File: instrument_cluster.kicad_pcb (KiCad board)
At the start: 2 copper layers, 144.8 x 45.7 mm, 76 parts, among them J1 Conn_02x16_Top_Bottom, J2 Conn_02x16_Top_Bottom, J3 USB mini-B SMD, J4 NOT_FITTED_SWD_Conn_01x04_Male, J5 54819-0572, J6 NOT_FITTED_SWD_Conn_01x04_Male, U1 LM2575S-5.0_NOPB, U10 74HC4050D, U11 TJA1040T, U12 TJA1040T, U2 LM2575S-5.0_NOPB, U3 LD1117S33TR_SOT223, U4 LD1117S33TR_SOT223, U5 STM32F105RBTx, U6 TJA1040T, U7 TJA1040T, U8 74HC4050D, U9 STM32F105RBTx, Y1 Crystal KX-13 25MHz, Y2 Crystal KX-13 25MHz

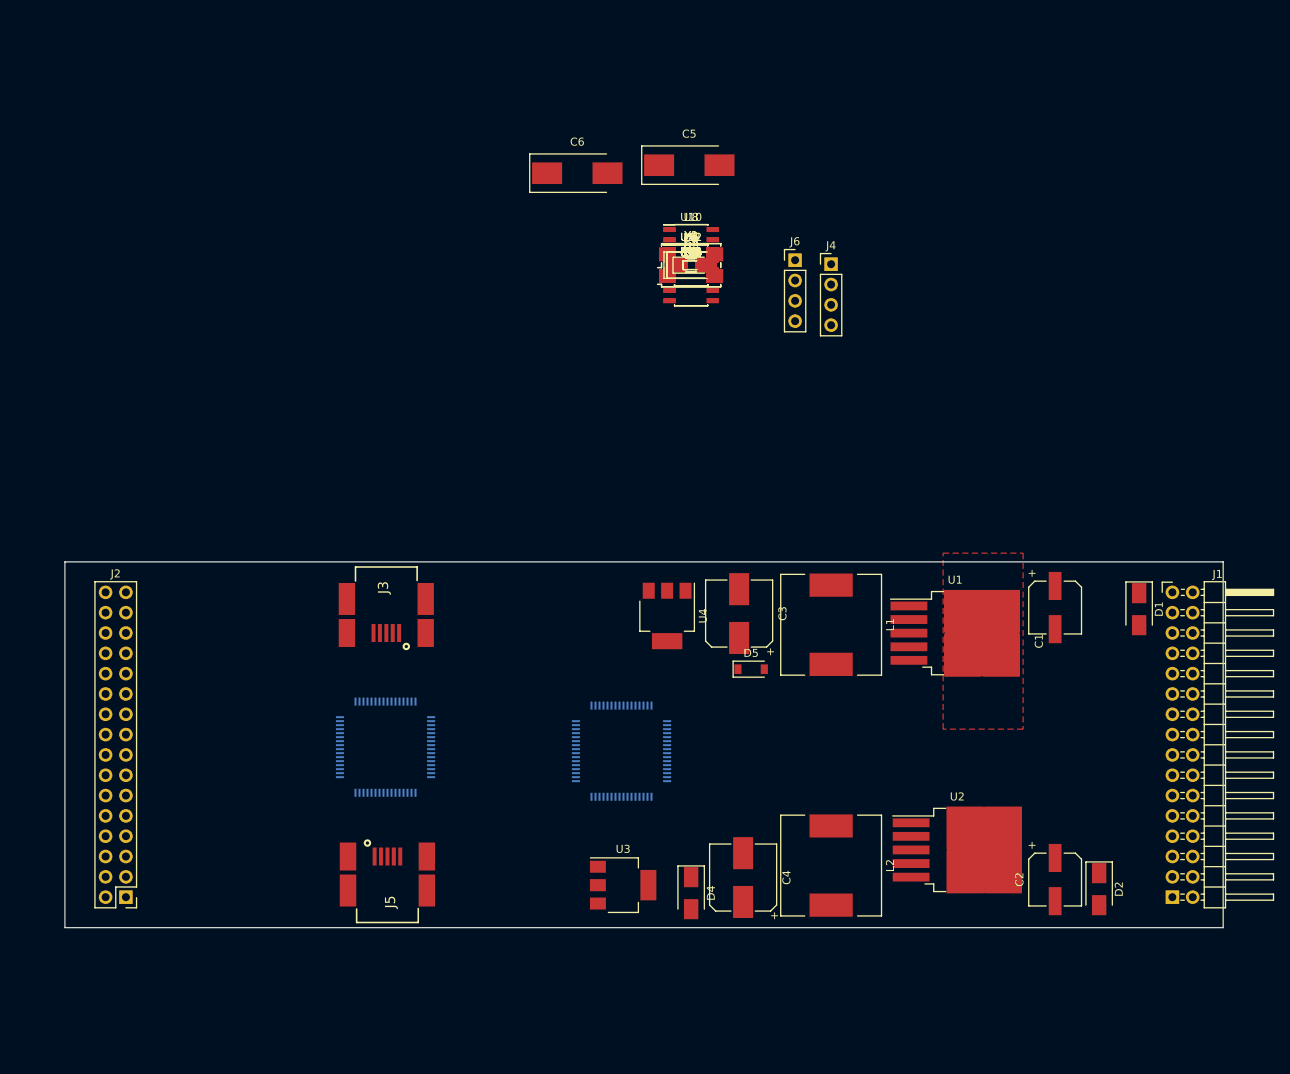
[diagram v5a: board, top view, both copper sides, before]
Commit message: power converters placement complete
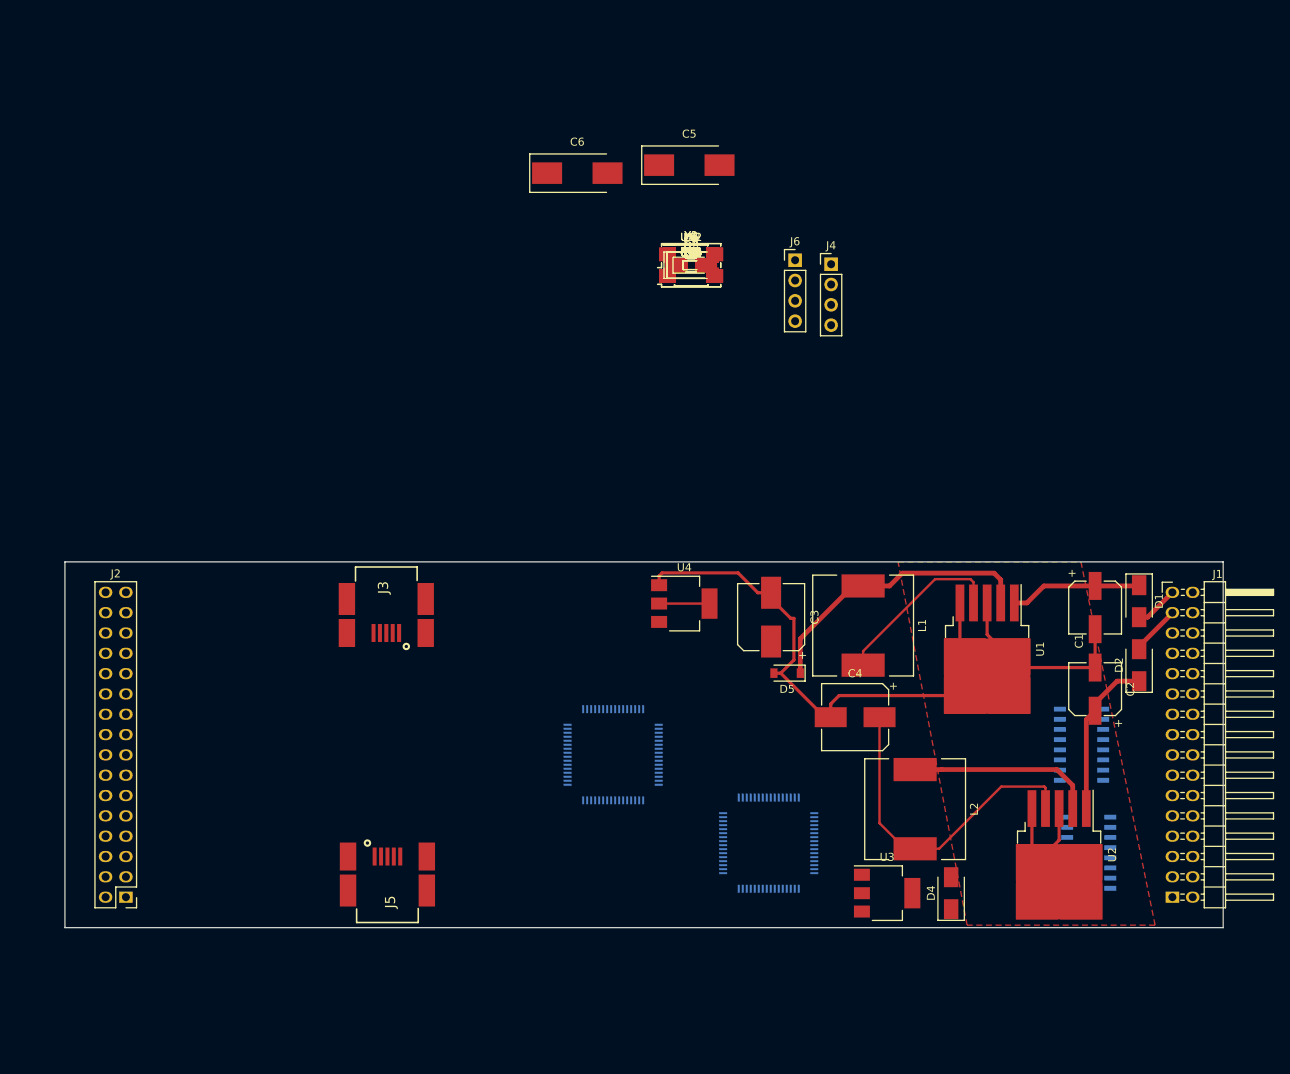
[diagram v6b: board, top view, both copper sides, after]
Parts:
- U10, U8: moved to B.Cu
- moved U8 88.7 mm to (190.2, 121.4), turned to 180 degrees
- moved U10 77.3 mm to (189.3, 107.9), turned to 180 degrees
- moved U9 49.4 mm to (150.2, 120.2)
- moved U3 33.0 mm to (165.0, 126.5)
- moved D4 32.5 mm to (173.0, 126.5), turned to 90 degrees
- moved D2 28.4 mm to (196.5, 98.0), turned to 90 degrees
- moved C4 24.5 mm to (161.0, 104.5), turned to 180 degrees
- moved C2 24.3 mm to (191.0, 101.0), turned to 90 degrees
- moved U2 12.7 mm to (186.5, 121.7), turned to 270 degrees
- moved L2 12.6 mm to (168.5, 116.0)
- moved C1 5.00 mm to (191.0, 90.8)
- moved D5 4.53 mm to (152.5, 99.0), turned to 180 degrees
- moved U1 4.47 mm to (177.5, 96.0), turned to 270 degrees
- moved C3 4.03 mm to (150.5, 92.0)
- moved L1 4.00 mm to (162.0, 93.0)
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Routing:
- net GND: track 0.00 -> 134.7 mm
- net /power_supply/+5V_A_module: track 0.00 -> 41.2 mm
- net Net-(D5-Pad1): track 0.00 -> 36.0 mm
- net Net-(D6-Pad1): track 0.00 -> 23.4 mm
- net /power_supply/+5V_B_module: track 0.00 -> 22.0 mm
- net /power_supply/+12V_A: track 0.00 -> 20.3 mm
- net /FUEL_TANK_in: track 0.00 -> 16.9 mm
- net /+3V3_B: track 0.00 -> 6.30 mm
- net /IGN: track 0.00 -> 6.28 mm
- net /VBATT: track 0.00 -> 5.44 mm

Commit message: change connectivity of level-shifters(on sheme and pcb)
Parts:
- moved U10 6.70 mm to (192.6, 113.8), turned to 270 degrees
- moved U8 2.59 mm to (192.4, 122.8), turned to 270 degrees
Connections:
- J1 pad 10: (no net) -> Net-(J1-Pad10)
- J1 pad 11: (no net) -> Net-(J1-Pad11)
- J1 pad 14: (no net) -> Net-(J1-Pad14)
- J1 pad 20: (no net) -> /RR_FOG
- J1 pad 23: (no net) -> Net-(J1-Pad23)
- J1 pad 24: (no net) -> /FR_FOG
- J1 pad 25: (no net) -> Net-(J1-Pad25)
- J1 pad 26: (no net) -> Net-(J1-Pad26)
- J1 pad 28: (no net) -> Net-(J1-Pad28)
- J1 pad 29: (no net) -> Net-(J1-Pad29)
- J1 pad 30: (no net) -> Net-(J1-Pad30)
- J2 pad 10: (no net) -> Net-(J2-Pad10)
- J2 pad 11: (no net) -> Net-(J2-Pad11)
- J2 pad 13: (no net) -> Net-(J2-Pad13)
- J2 pad 14: (no net) -> Net-(J2-Pad14)
- J2 pad 16: (no net) -> Net-(J2-Pad16)
- J2 pad 17: (no net) -> Net-(J2-Pad17)
- J2 pad 18: (no net) -> Net-(J2-Pad18)
- J2 pad 19: (no net) -> Net-(J2-Pad19)
- J2 pad 2: (no net) -> Net-(J2-Pad2)
- J2 pad 20: (no net) -> Net-(J2-Pad20)
- J2 pad 22: (no net) -> Net-(J2-Pad22)
- J2 pad 24: (no net) -> Net-(J2-Pad24)
- J2 pad 25: (no net) -> Net-(J2-Pad25)
- J2 pad 26: (no net) -> Net-(J2-Pad26)
- J2 pad 27: (no net) -> Net-(J2-Pad27)
- J2 pad 28: (no net) -> /LIN_(contact_spiral)
- J2 pad 29: (no net) -> Net-(J2-Pad29)
- J2 pad 3: (no net) -> Net-(J2-Pad3)
- J2 pad 30: (no net) -> Net-(J2-Pad30)
- J2 pad 31: (no net) -> /ESCL
- J2 pad 32: (no net) -> Net-(J2-Pad32)
- J2 pad 4: (no net) -> Net-(J2-Pad4)
- J2 pad 6: (no net) -> Net-(J2-Pad6)
- J2 pad 8: (no net) -> Net-(J2-Pad8)
- J3 pad 4: (no net) -> Net-(J3-Pad4)
- J5 pad 4: (no net) -> Net-(J5-Pad4)
- R11 pad 1: /FUEL_TANK_out1 -> /Module B (2can_filter+extra)/stm_adc_1
- R12 pad 1: /FUEL_TANK_out2 -> /Module B (2can_filter+extra)/stm_adc_2
- R13 pad 2: /FUEL_TANK_out1 -> /Module B (2can_filter+extra)/stm_adc_1
- R14 pad 2: /FUEL_TANK_out2 -> /Module B (2can_filter+extra)/stm_adc_2
- U10 pad 10: /Module B (2can_filter+extra)/washer -> /Module B (2can_filter+extra)/belt
- U10 pad 11: /ENGINE(coolant_level) -> Net-(U10-Pad11)
- U10 pad 12: /Module B (2can_filter+extra)/engine_coolant -> Net-(U10-Pad12)
- U10 pad 13: (no net) -> Net-(U10-Pad13)
- U10 pad 14: (no net) -> /ANTI-THEFT
- U10 pad 15: (no net) -> /Module B (2can_filter+extra)/anti-theft_stm
- U10 pad 16: (no net) -> Net-(U10-Pad16)
- U10 pad 2: /Module B (2can_filter+extra)/trip_comp -> /Module B (2can_filter+extra)/pad_wear
- U10 pad 3: /TRIP_COMPUTER -> /PAD-WEAR
- U10 pad 4: /ILLUM -> Net-(U10-Pad4)
- U10 pad 5: /ILLUM -> Net-(U10-Pad5)
- U10 pad 6: /ANTI-THEFT -> /Module B (2can_filter+extra)/parking_brakes
- U10 pad 7: /ANTI-THEFT -> /PARKING_BRAKE
- U10 pad 9: /LAW_WASHER(fluid_level) -> /BELT_MINDER
- U5 pad 10: (no net) -> Net-(U5-Pad10)
- U5 pad 11: (no net) -> Net-(U5-Pad11)
- U5 pad 14: (no net) -> Net-(U5-Pad14)
- U5 pad 15: (no net) -> Net-(U5-Pad15)
- U5 pad 16: (no net) -> Net-(U5-Pad16)
- U5 pad 17: (no net) -> Net-(U5-Pad17)
- U5 pad 2: (no net) -> Net-(U5-Pad2)
- U5 pad 20: (no net) -> Net-(U5-Pad20)
- U5 pad 21: (no net) -> Net-(U5-Pad21)
- U5 pad 22: (no net) -> Net-(U5-Pad22)
- U5 pad 23: (no net) -> Net-(U5-Pad23)
- U5 pad 24: (no net) -> Net-(U5-Pad24)
- U5 pad 25: (no net) -> Net-(U5-Pad25)
- U5 pad 26: (no net) -> Net-(U5-Pad26)
- U5 pad 27: (no net) -> Net-(U5-Pad27)
- U5 pad 28: (no net) -> Net-(U5-Pad28)
- U5 pad 29: (no net) -> Net-(U5-Pad29)
- U5 pad 3: (no net) -> Net-(U5-Pad3)
- U5 pad 30: (no net) -> Net-(U5-Pad30)
- U5 pad 33: (no net) -> Net-(U5-Pad33)
- U5 pad 34: (no net) -> Net-(U5-Pad34)
- U5 pad 35: (no net) -> Net-(U5-Pad35)
- U5 pad 36: (no net) -> Net-(U5-Pad36)
- U5 pad 37: (no net) -> Net-(U5-Pad37)
- U5 pad 38: (no net) -> Net-(U5-Pad38)
- U5 pad 39: (no net) -> Net-(U5-Pad39)
- U5 pad 4: (no net) -> Net-(U5-Pad4)
- U5 pad 40: (no net) -> Net-(U5-Pad40)
- U5 pad 41: (no net) -> Net-(U5-Pad41)
- U5 pad 43: (no net) -> Net-(U5-Pad43)
- U5 pad 50: (no net) -> Net-(U5-Pad50)
- U5 pad 51: (no net) -> Net-(U5-Pad51)
- U5 pad 52: (no net) -> Net-(U5-Pad52)
- U5 pad 53: (no net) -> Net-(U5-Pad53)
- U5 pad 54: (no net) -> Net-(U5-Pad54)
- U5 pad 55: (no net) -> Net-(U5-Pad55)
- U5 pad 56: (no net) -> Net-(U5-Pad56)
- U5 pad 59: (no net) -> Net-(U5-Pad59)
- U5 pad 60: (no net) -> Net-(U5-Pad60)
- U5 pad 7: (no net) -> Net-(U5-Pad7)
- U5 pad 8: (no net) -> Net-(U5-Pad8)
- U5 pad 9: (no net) -> Net-(U5-Pad9)
- U8 pad 10: /Module B (2can_filter+extra)/brake_fluid_level -> /Module B (2can_filter+extra)/engine_coolant
- U8 pad 11: /BELT_MINDER -> /OIL-pressure
- U8 pad 12: /Module B (2can_filter+extra)/belt -> /Module B (2can_filter+extra)/oil_pressure_level
- U8 pad 13: (no net) -> Net-(U8-Pad13)
- U8 pad 14: (no net) -> /LAW_WASHER(fluid_level)
- U8 pad 15: (no net) -> /Module B (2can_filter+extra)/washer
- U8 pad 16: (no net) -> Net-(U8-Pad16)
- U8 pad 2: /Module B (2can_filter+extra)/pad_wear -> /Module B (2can_filter+extra)/brake_fluid_level
- U8 pad 3: /PAD-WEAR -> /BRAKE(fluid_level)
- U8 pad 4: /Module B (2can_filter+extra)/oil_pressure_level -> /Module B (2can_filter+extra)/illum_stm
- U8 pad 5: /OIL-pressure -> /ILLUM
- U8 pad 6: /Module B (2can_filter+extra)/parking_brakes -> /Module B (2can_filter+extra)/trip_comp
- U8 pad 7: /PARKING_BRAKE -> /TRIP_COMPUTER
- U8 pad 9: /BRAKE(fluid_level) -> /ENGINE(coolant_level)
- U9 pad 10: (no net) -> Net-(U9-Pad10)
- U9 pad 11: /FUEL_TANK_out2 -> /Module B (2can_filter+extra)/stm_adc_2
- U9 pad 14: (no net) -> Net-(U9-Pad14)
- U9 pad 15: /FUEL_TANK_out1 -> /Module B (2can_filter+extra)/stm_adc_1
- U9 pad 16: (no net) -> Net-(U9-Pad16)
- U9 pad 2: (no net) -> Net-(U9-Pad2)
- U9 pad 20: (no net) -> Net-(U9-Pad20)
- U9 pad 25: (no net) -> Net-(U9-Pad25)
- U9 pad 26: (no net) -> Net-(U9-Pad26)
- U9 pad 27: (no net) -> Net-(U9-Pad27)
- U9 pad 28: (no net) -> Net-(U9-Pad28)
- U9 pad 29: (no net) -> /Module B (2can_filter+extra)/LIN_TXD
- U9 pad 3: (no net) -> Net-(U9-Pad3)
- U9 pad 30: (no net) -> /Module B (2can_filter+extra)/LIN_RXD
- U9 pad 33: (no net) -> /Module B (2can_filter+extra)/LIN_SLP
- U9 pad 34: (no net) -> Net-(U9-Pad34)
- U9 pad 35: (no net) -> Net-(U9-Pad35)
- U9 pad 36: (no net) -> Net-(U9-Pad36)
- U9 pad 39: /ANTI-THEFT -> /Module B (2can_filter+extra)/anti-theft_stm
- U9 pad 4: (no net) -> Net-(U9-Pad4)
- U9 pad 40: /ILLUM -> /Module B (2can_filter+extra)/illum_stm
- U9 pad 41: (no net) -> Net-(U9-Pad41)
- U9 pad 43: (no net) -> Net-(U9-Pad43)
- U9 pad 50: (no net) -> Net-(U9-Pad50)
- U9 pad 51: (no net) -> Net-(U9-Pad51)
- U9 pad 53: (no net) -> Net-(U9-Pad53)
- U9 pad 54: (no net) -> Net-(U9-Pad54)
- U9 pad 55: (no net) -> Net-(U9-Pad55)
- U9 pad 56: (no net) -> Net-(U9-Pad56)
- U9 pad 59: (no net) -> Net-(U9-Pad59)
- U9 pad 60: (no net) -> Net-(U9-Pad60)
- U9 pad 7: (no net) -> Net-(U9-Pad7)
- U9 pad 8: (no net) -> Net-(U9-Pad8)
- U9 pad 9: (no net) -> Net-(U9-Pad9)
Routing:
- net /MS_CAN_L: track 0.00 -> 40.4 mm
- net /MS_CAN_H: track 0.00 -> 34.8 mm
- net /HS_CAN_L: track 0.00 -> 32.4 mm
- net /HS_CAN_H: track 0.00 -> 31.1 mm
- net GND: track 134.7 -> 159.1 mm, vias 0 -> 2
- net /BRAKE(fluid_level): track 0.00 -> 18.1 mm
- net /ANTI-THEFT: track 0.00 -> 17.6 mm
- net /LAW_WASHER(fluid_level): track 0.00 -> 13.5 mm
- net /PAD-WEAR: track 0.00 -> 12.6 mm
- net /ILLUM: track 0.00 -> 12.2 mm
- net /TRIP_COMPUTER: track 0.00 -> 11.6 mm
- net /Module B (2can_filter+extra)/belt: track 0.00 -> 10.9 mm
- net /Module B (2can_filter+extra)/engine_coolant: track 0.00 -> 10.5 mm
- net /Module B (2can_filter+extra)/trip_comp: track 0.00 -> 9.53 mm
- net /Module B (2can_filter+extra)/parking_brakes: track 0.00 -> 9.51 mm
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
